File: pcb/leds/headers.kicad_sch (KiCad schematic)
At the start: 4 parts, among them J1 QSH-060-01-L-D-A, J2 QSH-060-01-L-D-A, J3 QTH-060-01-L-D-A, J4 QTH-060-01-L-D-A

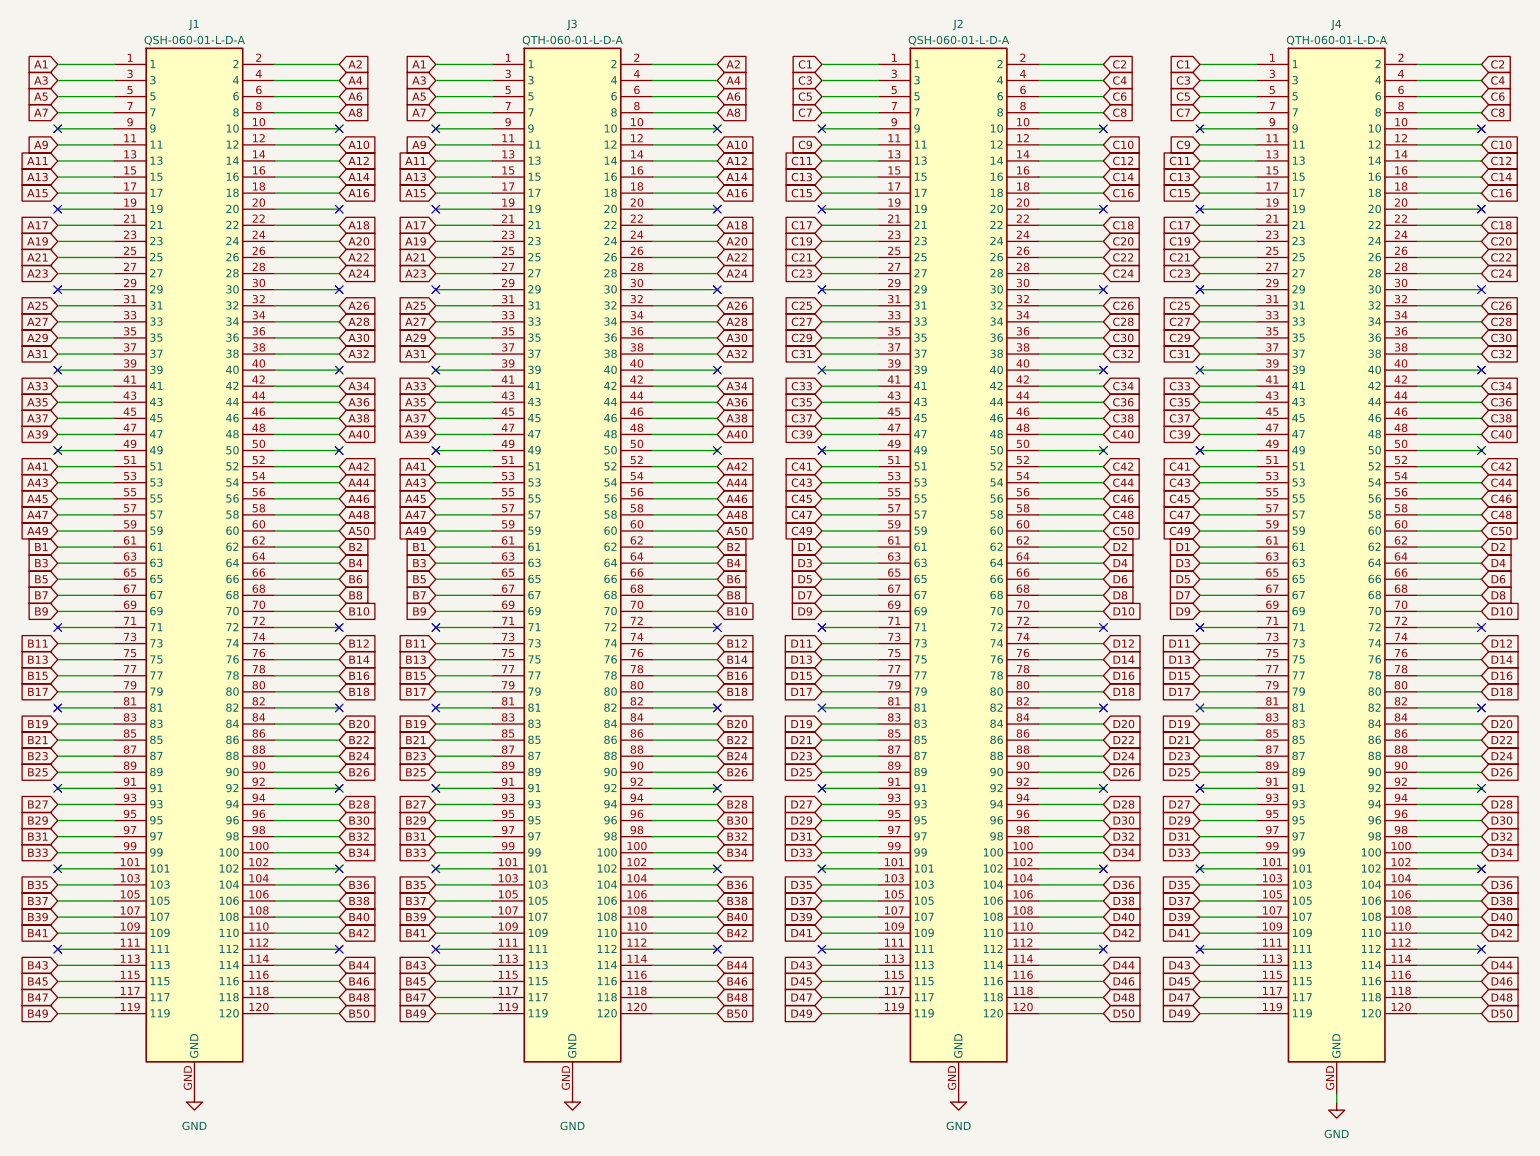
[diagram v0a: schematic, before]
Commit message: [pcb][leds] starting placement
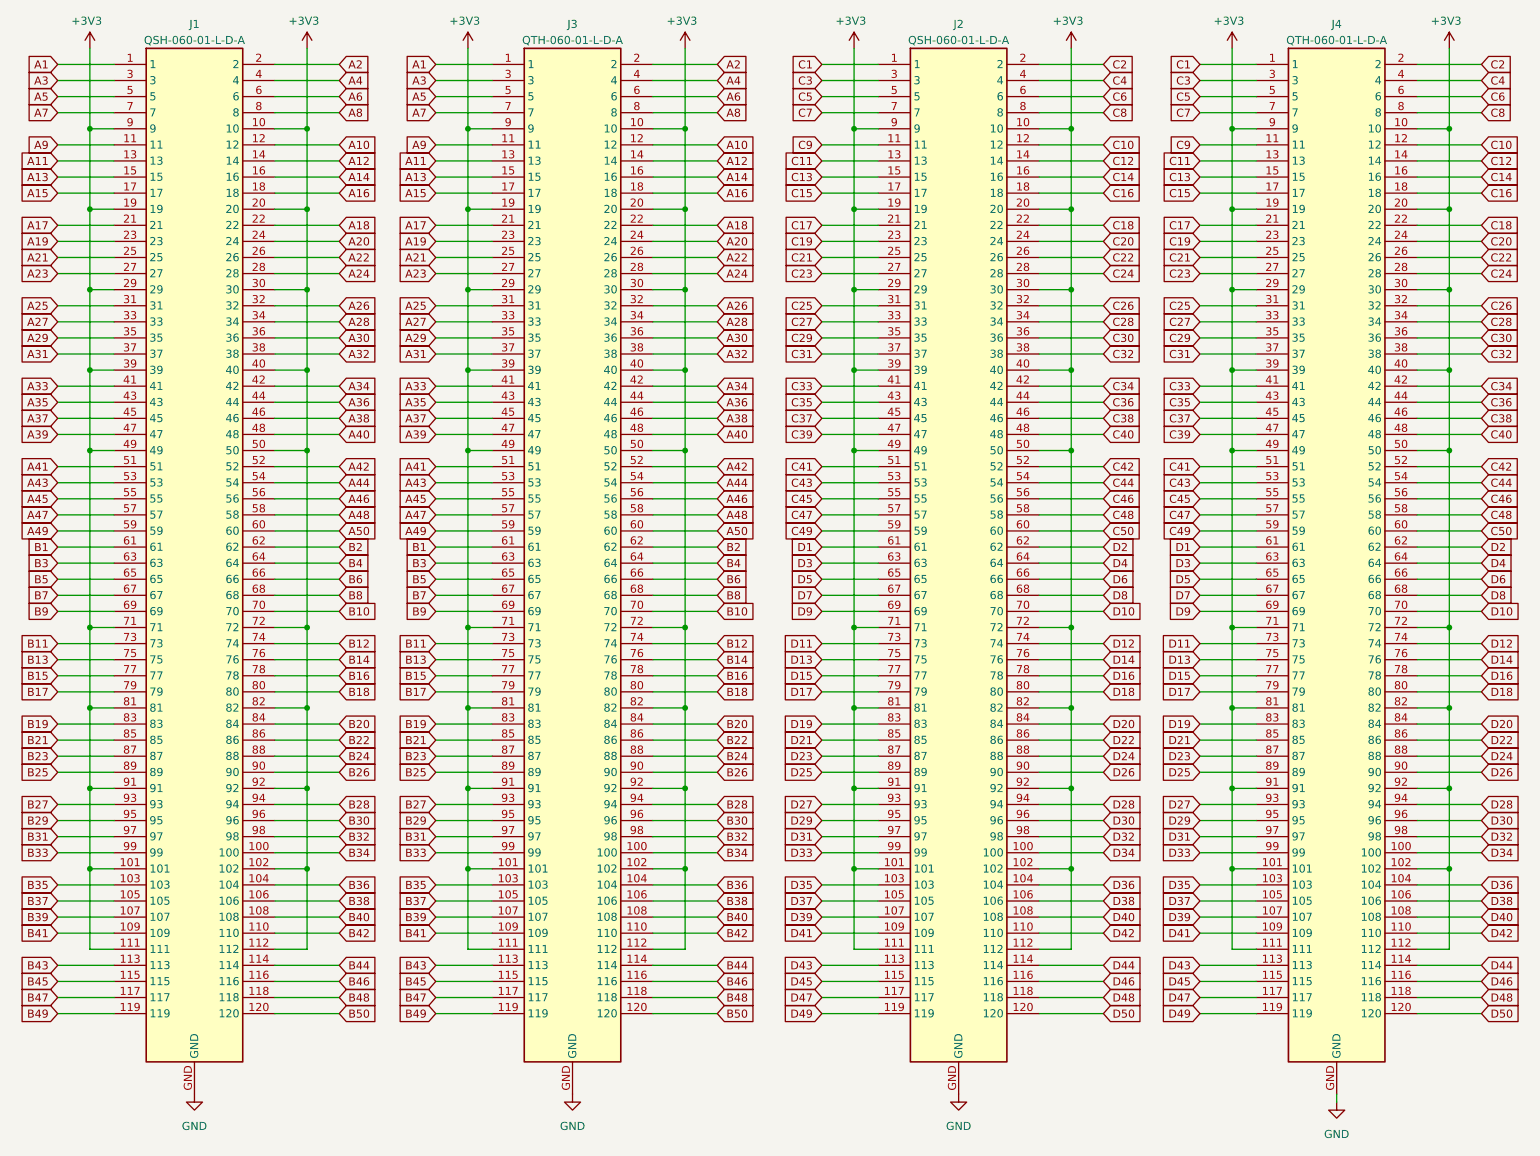
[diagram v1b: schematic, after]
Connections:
- net +3V3: now reaches J3.10
- net +3V3: now also J1.10, J1.101, J1.102, J1.111, J1.112, J1.19, J1.20, J1.29, J1.30, J1.39, J1.40, J1.49, J1.50, J1.71, J1.72, J1.81, J1.82, J1.9, J1.91, J1.92, J2.10, J2.101, J2.102, J2.111, J2.112, J2.19, J2.20, J2.29, J2.30, J2.39, J2.40, J2.49, J2.50, J2.71, J2.72, J2.81, J2.82, J2.9, J2.91, J2.92, J3.101, J3.102, J3.111, J3.112, J3.19, J3.20, J3.29, J3.30, J3.39, J3.40, J3.49, J3.50, J3.71, J3.72, J3.81, J3.82, J3.9, J3.91, J3.92, J4.10, J4.101, J4.102, J4.111, J4.112, J4.19, J4.20, J4.29, J4.30, J4.39, J4.40, J4.49, J4.50, J4.71, J4.72, J4.81, J4.82, J4.9, J4.91, J4.92
- no-connect marks 80 -> 0

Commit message: [pcb][leds] left side routed
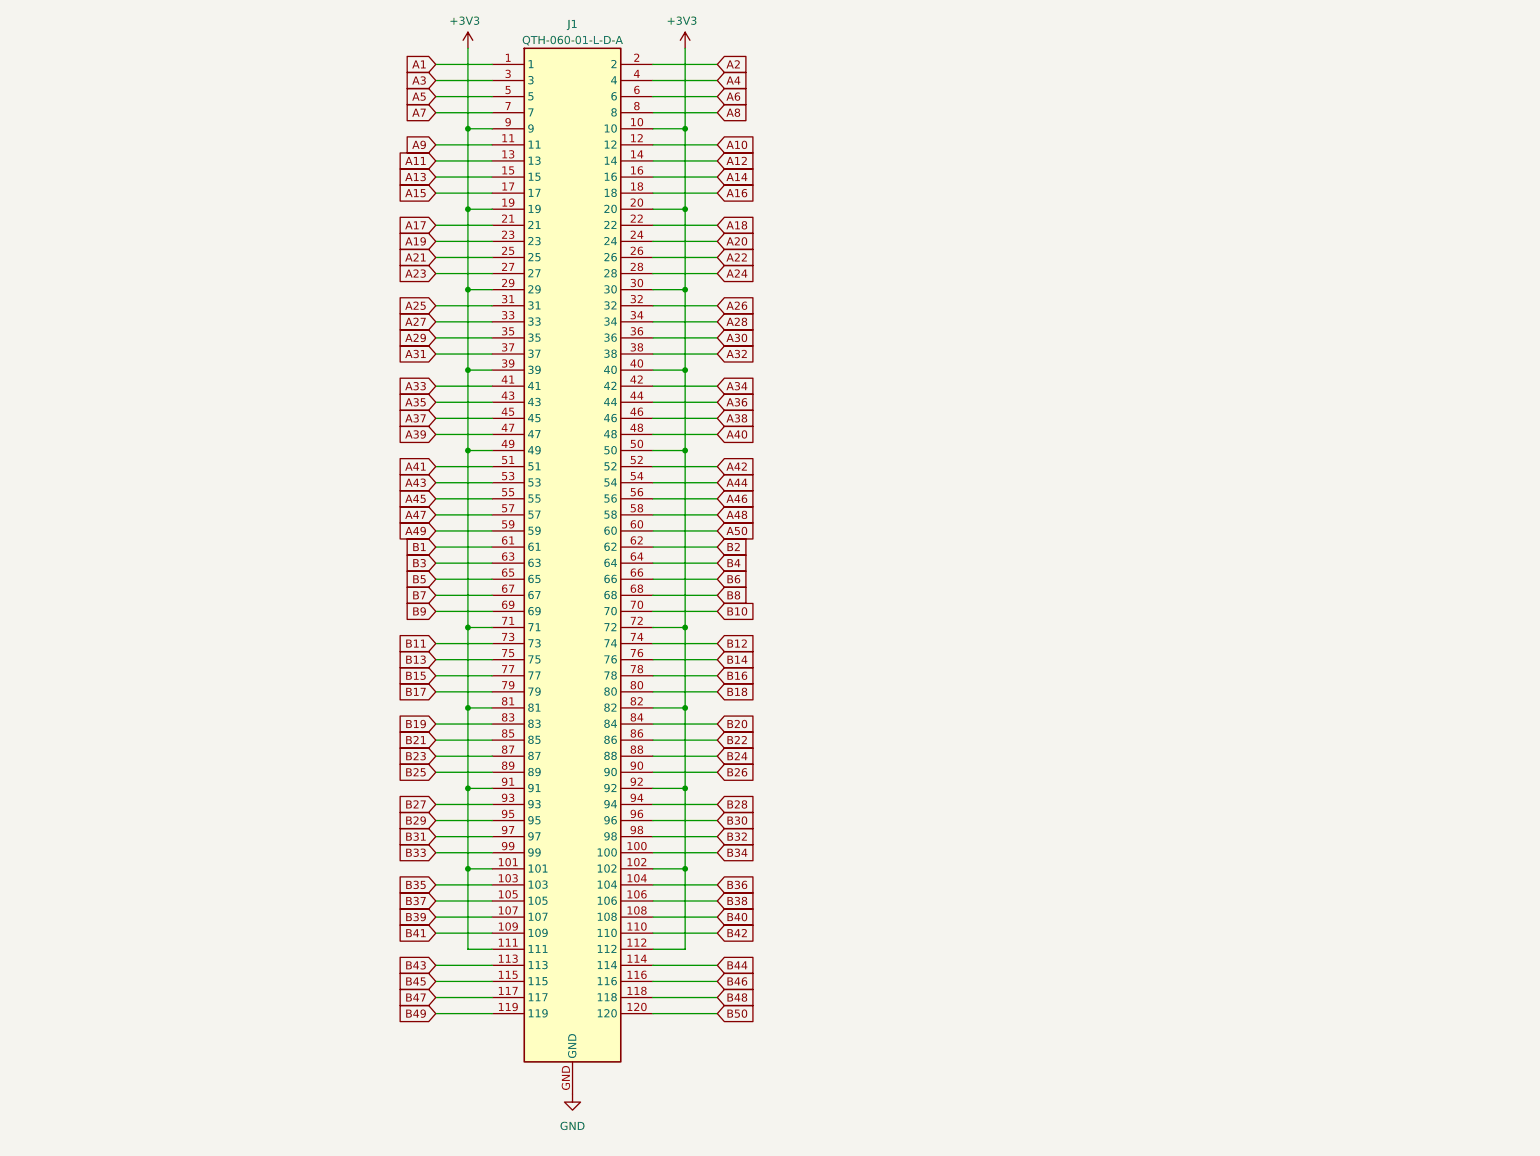
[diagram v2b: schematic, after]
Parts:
- removed J1, J2: QSH-060-01-L-D-A, !Misc:SAMTEC_QSH-060-01-X-D-A, symbol !Misc:QSH-060-01-L-D-A
- removed J4: QTH-060-01-L-D-A, !Misc:SAMTEC_QTH-060-01-X-D-A, symbol !Misc:QTH-060-01-L-D-A
- renumbered J3 to J1
